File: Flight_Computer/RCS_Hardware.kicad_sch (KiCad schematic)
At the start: 68 parts, among them J1 SWD, J10 Motor, J2 TYPE-C-31-M-12, J3 I2C, J4 5V, J5 GND, J6 AMT102, J7 FC_RF, J9 AMT102, Q1 2N7002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

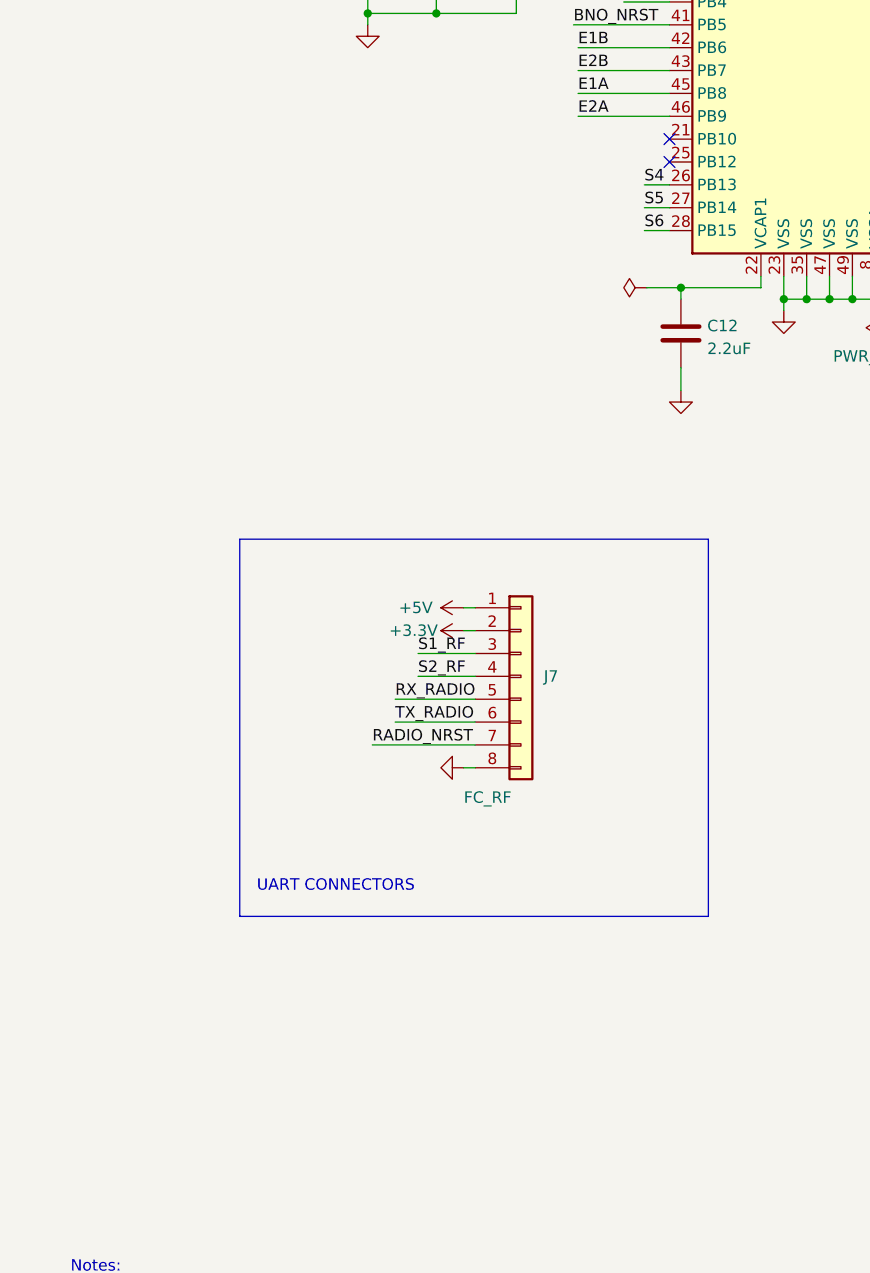
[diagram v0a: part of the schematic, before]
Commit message: added and started wiring temp sensor chip
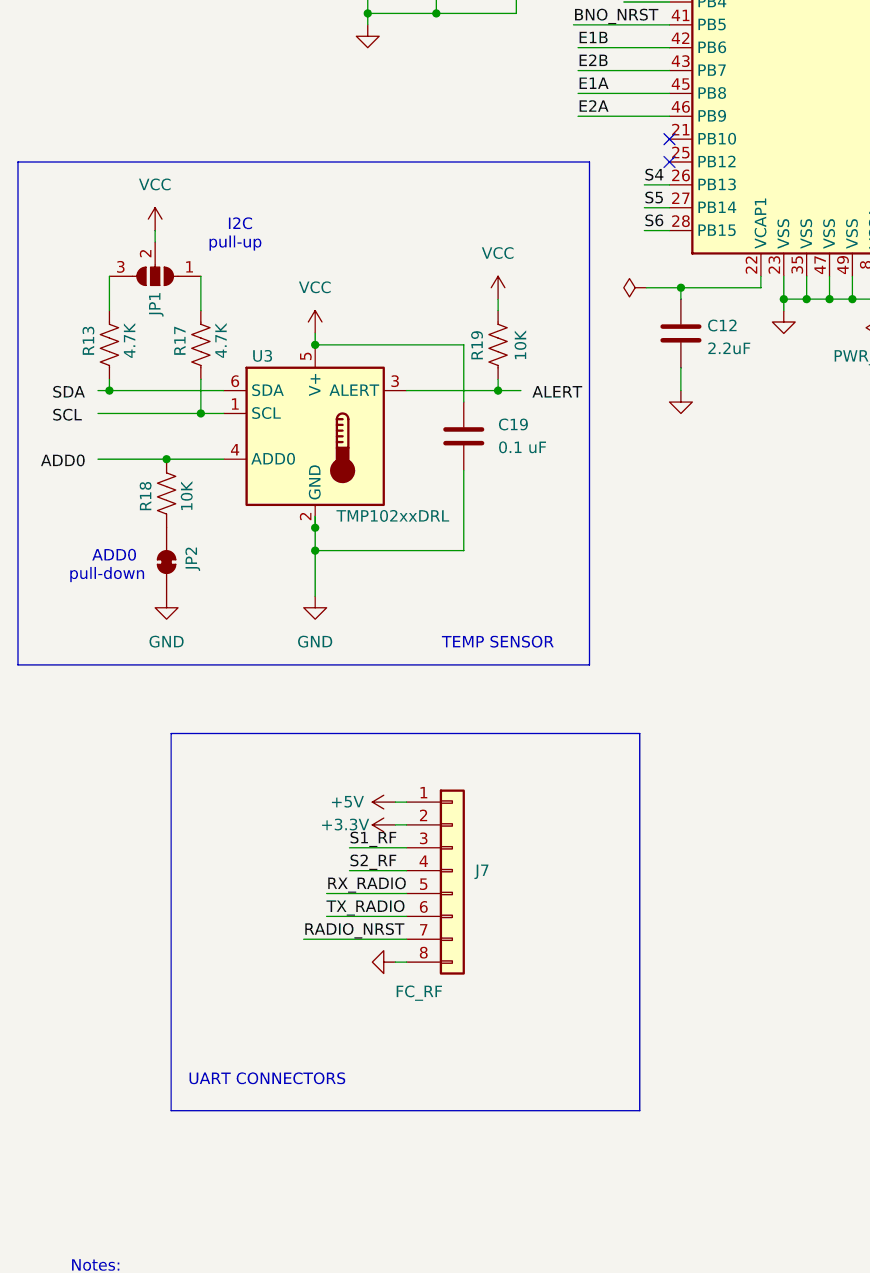
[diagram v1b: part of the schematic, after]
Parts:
- added C19: 0.1 uF, symbol Device:C
- added JP1: SolderJumper_3_Open, symbol Jumper:SolderJumper_3_Open
- added JP2: SolderJumper_2_Bridged, symbol Jumper:SolderJumper_2_Bridged
- added R13, R17: 4.7K, symbol Device:R_US
- added R18, R19: 10K, symbol Device:R_US
- added U3: TMP102xxDRL, Package_TO_SOT_SMD:SOT-563, symbol Sensor_Temperature:TMP102xxDRL
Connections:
- net GND: now also C19.2, JP2.1 (A), U3.2 (GND)
- net VCC: now also C19.1, JP1.2 (C), R19.1, U3.5 (V+)
- new net: R17.2, U3.1 (SCL)
- new net: R19.2, U3.3 (ALERT)
- new net: R18.1, U3.4 (ADD0)
- new net: R13.2, U3.6 (SDA)
- new net: JP2.2 (B), R18.2
- new net: JP1.3 (B), R13.1
- new net: JP1.1 (A), R17.1
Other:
- note added: "ADD0 pull-down"
- note added: "I2C pull-up"
- note added: "TEMP SENSOR"
- moved on the sheet: J7

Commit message: modified temp sensor connections
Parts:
- removed JP1: SolderJumper_3_Open, symbol Jumper:SolderJumper_3_Open
- removed JP2: SolderJumper_2_Bridged, symbol Jumper:SolderJumper_2_Bridged
- removed R13, R17: 4.7K, symbol Device:R_US
- removed R18, R19: 10K, symbol Device:R_US
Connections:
- net GND: now also U3.4 (ADD0)
- no-connect marks 15 -> 16
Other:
- note removed: "ADD0 pull-down"
- note removed: "I2C pull-up"
